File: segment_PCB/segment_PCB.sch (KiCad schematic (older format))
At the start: 36 parts, among them J2 #AVR-ISP-6, SW1 SW_Push, U4 74HC138, Y1 12MHz

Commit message: Started mock keyboard
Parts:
- removed C8, C?: 100n, Capacitor_THT:C_Disc_D3.0mm_W1.6mm_P2.50mm, symbol Device:C
- removed D4: LED, LED_THT:LED_D5.0mm, symbol Device:LED
- removed R7: R, Resistor_THT:R_Axial_DIN0204_L3.6mm_D1.6mm_P5.08mm_Horizontal, symbol Device:R
- removed SW? (x6): SW_Push, symbol Switch:SW_Push
- removed U?: 74HC138, symbol Segment_Parts:74HC138
- removed U?: 74HC365, symbol Segment_Parts:74HC365
- added C?: 100n, Capacitor_THT:C_Disc_D3.0mm_W1.6mm_P2.50mm, symbol Device:C
- added R? (x5): 10k, symbol Device:R
- added SW? (x5): SW_Push_45deg, symbol Switch:SW_Push_45deg
- added U?: 74HC365, symbol Segment_Parts:74HC365
- R6: value R -> 220R
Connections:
- net SEL4 is gone; now on net GND: U4.4 (~E1), U?.5 (~E2)
- net CBUS: now also U?.15 (~Y0), U?.15 (~E2)
- net COL1: no longer U?.6 (PD4)
- net COL2: no longer U?.11 (PD5)
- net COL3: no longer U?.12 (PD6)
- net COL4: no longer U?.13 (PD7)
- net GND: now also C?.2, U?.1 (~E1), U?.10 (A4), U?.12 (A5), U?.14 (A6), U?.2 (A1), U?.4 (A2), U?.6 (A3), U?.8 (GND)
- net LED0: now also U?.16 (PB2)
- net ROW0: now also R?.2, SW?.2
- net ROW1: now also R?.2, SW?.2
- net ROW2: now also R?.2, SW?.2
- net ROW3: now also R?.2, SW?.2
- net ROW4: now also R?.2, SW?.2
- net SEL0: now also U?.5 (PD3)
- net SEL1: now also U?.6 (PD4)
- net SEL2: now also U?.11 (PD5)
- net SEL3: now also U?.12 (PD6)
- net VCC: now also C?.1, R?.1, R?.1, R?.1, R?.1, R?.1, U?.16 (VCC)
- removed net COL0: U?.15 (~Y0), U?.5 (PD3)
- net COL14: no longer names the net of U4.9 (~Y6)
- net COL15: no longer names the net of U4.7 (~Y7)
- net ROW5: no longer names the net of U?.26 (PC3)
- new net: SW?.1, U?.11 (Y5)
- new net: SW?.1, U?.3 (Y1)
- new net: SW?.1, U?.5 (Y2)
- new net: SW?.1, U?.7 (Y3)
- new net: SW?.1, U?.9 (Y4)
- no-connect marks 2 -> 5
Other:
- moved on the sheet: C3, C4, C5, C6, C7, C?, D3, D?, F?, J2, J?, R5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

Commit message: Completed test board layout; implementing option footprints
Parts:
- U4, U?: symbol Segment_Parts:74HC138 -> Segment_Symbols:74HC138
- U?: symbol Segment_Parts:74HC365 -> Segment_Symbols:74HC365
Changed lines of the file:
@@
 	3400 2200 3400 2500
 $Comp
-L Segment_Parts:74HC138 U4
+L Segment_Symbols:74HC138 U4
 U 1 1 5FB534DC
 P 4050 2000
@@
 	13200 8600 13200 8500
 $Comp
-L Segment_Parts:74HC138 U?
+L Segment_Symbols:74HC138 U?
 U 1 1 5FBECC10
 P 1950 2000
@@
 	5400 4700 5350 4700
 $Comp
-L Segment_Parts:74HC365 U?
+L Segment_Symbols:74HC365 U?
 U 1 1 604297EC
 P 5800 5100

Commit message: Minor tweak to test board
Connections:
- net at U?.11 (Y5): now also SW?.1; no longer SW?.1
- net at U?.13 (Y6): now also SW?.1
- net at U?.3 (Y1): no longer SW?.1
- net at U?.5 (Y2): now also SW?.1; no longer SW?.1
- net at U?.7 (Y3): now also SW?.1; no longer SW?.1
- net at U?.9 (Y4): now also SW?.1; no longer SW?.1
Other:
- moved on the sheet: SW?
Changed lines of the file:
@@
 Connection ~ 13200 8300
 NoConn ~ 4450 2300
-Text GLabel 6650 5650 3    50   Input ~ 0
+Text GLabel 6600 5650 3    50   Input ~ 0
 ROW3
-Text GLabel 6850 5650 3    50   Input ~ 0
+Text GLabel 6800 5650 3    50   Input ~ 0
 ROW2
-Text GLabel 7050 5650 3    50   Input ~ 0
+Text GLabel 7000 5650 3    50   Input ~ 0
 ROW1
-Text GLabel 7250 5650 3    50   Input ~ 0
+Text GLabel 7200 5650 3    50   Input ~ 0
 ROW0
 $Comp
 L Switch:SW_Push_45deg SW?
 U 1 1 60429834
-P 7150 4800
-F 0 "SW?" V 7200 4600 50  0000 C CNN
-F 1 "SW_Push_45deg" H 7150 4990 50  0001 C CNN
-F 2 "" H 7150 4800 50  0001 C CNN
-F 3 "~" H 7150 4800 50  0001 C CNN
-	1    7150 4800
-	1    0    0    -1
-$EndComp
-Wire Wire Line
-	6650 5650 6650 5200
+P 7100 4900
+F 0 "SW?" V 7150 4700 50  0000 C CNN
+F 1 "SW_Push_45deg" H 7100 5090 50  0001 C CNN
+F 2 "" H 7100 4900 50  0001 C CNN
+F 3 "~" H 7100 4900 50  0001 C CNN
+	1    7100 4900
+	1    0    0    -1
+$EndComp
 $Comp
 L Switch:SW_Push_45deg SW?
 U 1 1 60429845
-P 6950 4900
-F 0 "SW?" V 7000 4700 50  0000 C CNN
-F 1 "SW_Push_45deg" H 6950 5090 50  0001 C CNN
-F 2 "" H 6950 4900 50  0001 C CNN
-F 3 "~" H 6950 4900 50  0001 C CNN
-	1    6950 4900
+P 6900 5000
+F 0 "SW?" V 6950 4800 50  0000 C CNN
+F 1 "SW_Push_45deg" H 6900 5190 50  0001 C CNN
+F 2 "" H 6900 5000 50  0001 C CNN
+F 3 "~" H 6900 5000 50  0001 C CNN
+	1    6900 5000
 	1    0    0    -1
 $EndComp
@@
 L Switch:SW_Push_45deg SW?
 U 1 1 6042984B
-P 6750 5000
-F 0 "SW?" V 6800 4800 50  0000 C CNN
-F 1 "SW_Push_45deg" H 6750 5190 50  0001 C CNN
-F 2 "" H 6750 5000 50  0001 C CNN
-F 3 "~" H 6750 5000 50  0001 C CNN
-	1    6750 5000
-	1    0    0    -1
-$EndComp
-Wire Wire Line
-	7250 4900 7250 5650
-Wire Wire Line
-	7050 5650 7050 5000
-Wire Wire Line
-	6850 5100 6850 5650
+P 6700 5100
+F 0 "SW?" V 6750 4900 50  0000 C CNN
+F 1 "SW_Push_45deg" H 6700 5290 50  0001 C CNN
+F 2 "" H 6700 5100 50  0001 C CNN
+F 3 "~" H 6700 5100 50  0001 C CNN
+	1    6700 5100
+	1    0    0    -1
+$EndComp
 $Comp
 L Switch:SW_Push_45deg SW?
 U 1 1 60429857
-P 6350 5200
-F 0 "SW?" V 6400 5000 50  0000 C CNN
-F 1 "SW_Push_45deg" H 6350 5390 50  0001 C CNN
-F 2 "" H 6350 5200 50  0001 C CNN
-F 3 "~" H 6350 5200 50  0001 C CNN
-	1    6350 5200
+P 6300 5300
+F 0 "SW?" V 6350 5100 50  0000 C CNN
+F 1 "SW_Push_45deg" H 6300 5490 50  0001 C CNN
+F 2 "" H 6300 5300 50  0001 C CNN
+F 3 "~" H 6300 5300 50  0001 C CNN
+	1    6300 5300
 	1    0    0    -1
 $EndComp
@@
 L Switch:SW_Push_45deg SW?
 U 1 1 60429851
-P 6550 5100
-F 0 "SW?" V 6600 4900 50  0000 C CNN
-F 1 "SW_Push_45deg" H 6550 5290 50  0001 C CNN
-F 2 "" H 6550 5100 50  0001 C CNN
-F 3 "~" H 6550 5100 50  0001 C CNN
-	1    6550 5100
-	1    0    0    -1
-$EndComp
-Wire Wire Line
-	6450 5300 6450 5650
+P 6500 5200
+F 0 "SW?" V 6550 5000 50  0000 C CNN
+F 1 "SW_Push_45deg" H 6500 5390 50  0001 C CNN
+F 2 "" H 6500 5200 50  0001 C CNN
+F 3 "~" H 6500 5200 50  0001 C CNN
+	1    6500 5200
+	1    0    0    -1
+$EndComp
 Wire Wire Line
 	5350 5400 5350 5700
@@
 Wire Wire Line
 	5350 5200 5350 5400
-Text GLabel 6450 5650 3    50   Input ~ 0
+Text GLabel 6400 5650 3    50   Input ~ 0
 ROW4
 $Comp
@@
 NoConn ~ 13100 6250
 NoConn ~ 13100 5050
-NoConn ~ 6200 5200
-Wire Wire Line
-	6200 5100 6250 5100
-Wire Wire Line
-	6200 5000 6450 5000
-Wire Wire Line
-	6200 4900 6650 4900
-Wire Wire Line
-	6200 4800 6850 4800
-Wire Wire Line
-	6200 4700 7050 4700
+NoConn ~ 6200 4700
+Wire Wire Line
+	6200 5100 6400 5100
+Wire Wire Line
+	6200 5000 6600 5000
+Wire Wire Line
+	6200 4900 6800 4900
+Wire Wire Line
+	6200 4800 7000 4800
+Wire Wire Line
+	6400 5650 6400 5400
+Wire Wire Line
+	6600 5650 6600 5300
+Wire Wire Line
+	6800 5650 6800 5200
+Wire Wire Line
+	7000 5650 7000 5100
+Wire Wire Line
+	7200 5650 7200 5000
 Wire Bus Line
 	3250 1400 3250 2200

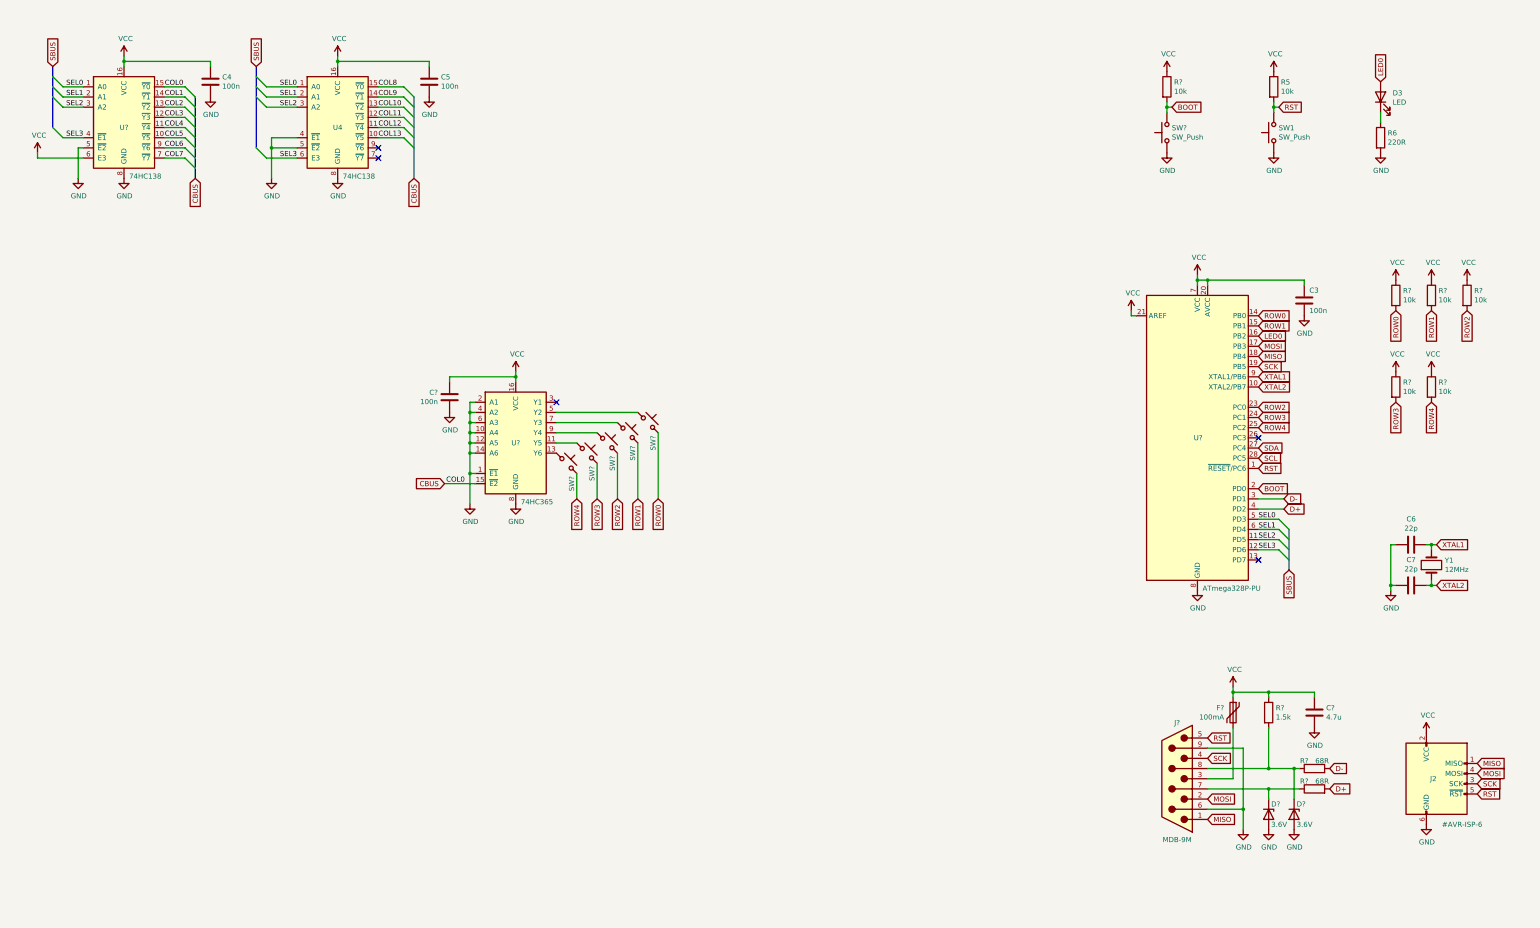
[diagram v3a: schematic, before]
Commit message: Added test board dimensions
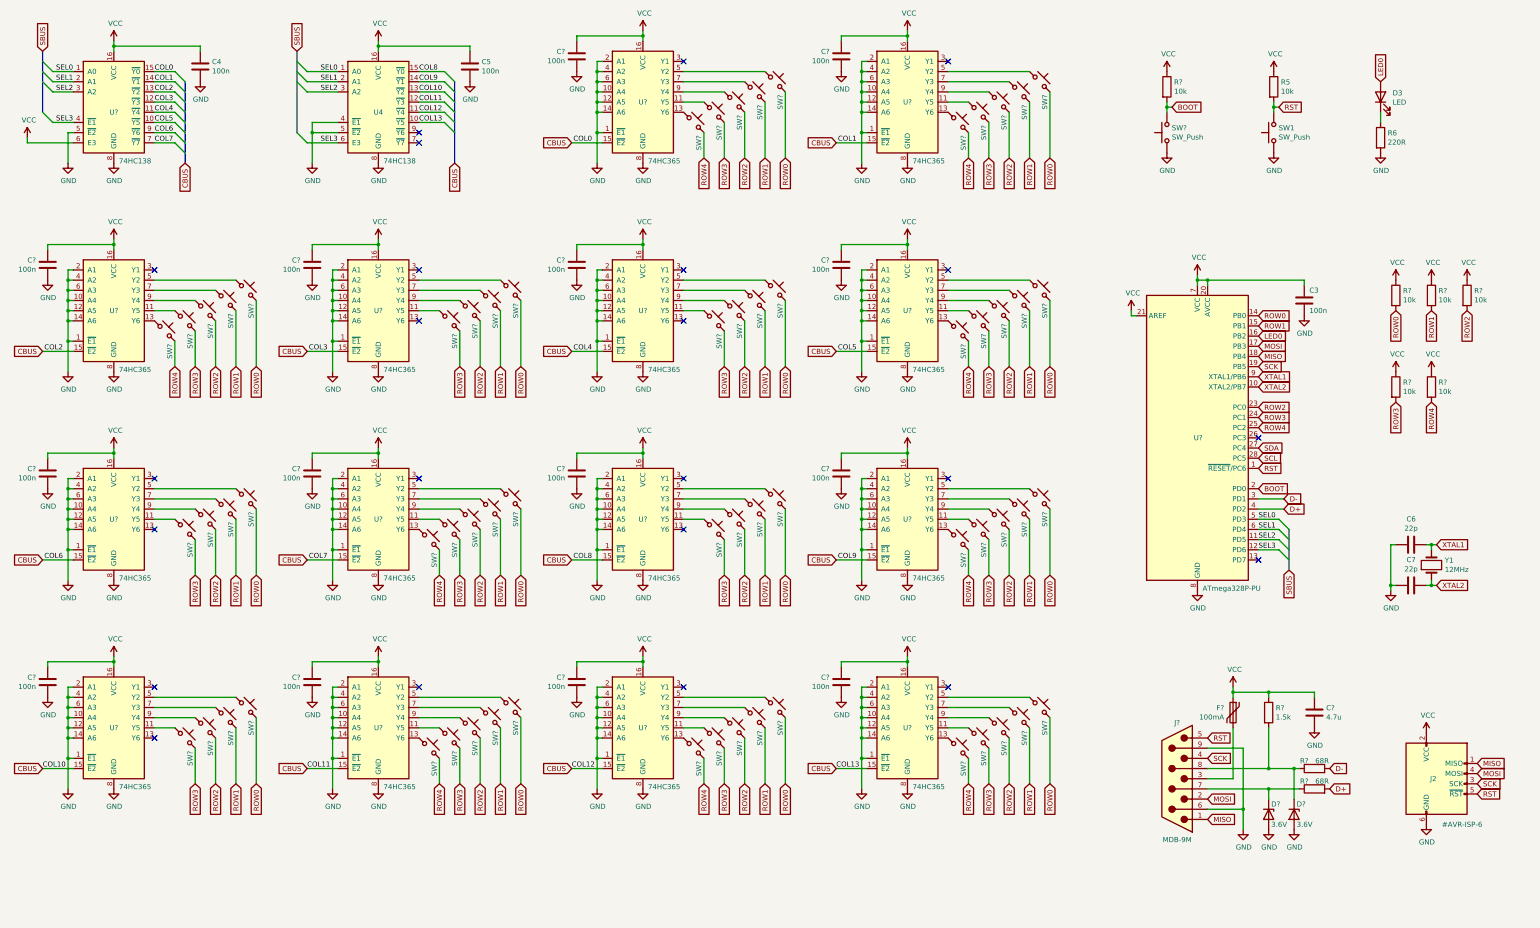
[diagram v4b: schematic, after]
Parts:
- added C? (x13): 100n, Capacitor_THT:C_Disc_D3.0mm_W1.6mm_P2.50mm, symbol Device:C
- added SW? (x60): SW_Push_45deg, symbol Switch:SW_Push_45deg
- added U? (x13): 74HC365, symbol Segment_Symbols:74HC365
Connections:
- net COL1 is gone; now on net CBUS: U?.14 (~Y1)
- net COL10 is gone; now on net CBUS: U4.13 (~Y2)
- net COL11 is gone; now on net CBUS: U4.12 (~Y3)
- net COL12 is gone; now on net CBUS: U4.11 (~Y4)
- net COL13 is gone; now on net CBUS: U4.10 (~Y5)
- net COL2 is gone; now on net CBUS: U?.13 (~Y2)
- net COL3 is gone; now on net CBUS: U?.12 (~Y3)
- net COL4 is gone; now on net CBUS: U?.11 (~Y4)
- net COL5 is gone; now on net CBUS: U?.10 (~Y5)
- net COL6 is gone; now on net CBUS: U?.9 (~Y6)
- net COL7 is gone; now on net CBUS: U?.7 (~Y7)
- net COL8 is gone; now on net CBUS: U4.15 (~Y0)
- net COL9 is gone; now on net CBUS: U4.14 (~Y1)
- net CBUS: now also U?.15 (~E2), U?.15 (~E2), U?.15 (~E2), U?.15 (~E2), U?.15 (~E2), U?.15 (~E2), U?.15 (~E2), U?.15 (~E2), U?.15 (~E2), U?.15 (~E2), U?.15 (~E2), U?.15 (~E2), U?.15 (~E2)
- net GND: now also C?.2, C?.2, C?.2, C?.2, C?.2, C?.2, C?.2, C?.2, C?.2, C?.2, C?.2, C?.2, C?.2, U?.1 (~E1), U?.1 (~E1), U?.1 (~E1), U?.1 (~E1), U?.1 (~E1), U?.1 (~E1), U?.1 (~E1), U?.1 (~E1), U?.1 (~E1), U?.1 (~E1), U?.1 (~E1), U?.1 (~E1), U?.1 (~E1), U?.10 (A4), U?.10 (A4), U?.10 (A4), U?.10 (A4), U?.10 (A4), U?.10 (A4), U?.10 (A4), U?.10 (A4), U?.10 (A4), U?.10 (A4), U?.10 (A4), U?.10 (A4), U?.10 (A4), U?.12 (A5), U?.12 (A5), U?.12 (A5), U?.12 (A5), U?.12 (A5), U?.12 (A5), U?.12 (A5), U?.12 (A5), U?.12 (A5), U?.12 (A5), U?.12 (A5), U?.12 (A5), U?.12 (A5), U?.14 (A6), U?.14 (A6), U?.14 (A6), U?.14 (A6), U?.14 (A6), U?.14 (A6), U?.14 (A6), U?.14 (A6), U?.14 (A6), U?.14 (A6), U?.14 (A6), U?.14 (A6), U?.14 (A6), U?.2 (A1), U?.2 (A1), U?.2 (A1), U?.2 (A1), U?.2 (A1), U?.2 (A1), U?.2 (A1), U?.2 (A1), U?.2 (A1), U?.2 (A1), U?.2 (A1), U?.2 (A1), U?.2 (A1), U?.4 (A2), U?.4 (A2), U?.4 (A2), U?.4 (A2), U?.4 (A2), U?.4 (A2), U?.4 (A2), U?.4 (A2), U?.4 (A2), U?.4 (A2), U?.4 (A2), U?.4 (A2), U?.4 (A2), U?.6 (A3), U?.6 (A3), U?.6 (A3), U?.6 (A3), U?.6 (A3), U?.6 (A3), U?.6 (A3), U?.6 (A3), U?.6 (A3), U?.6 (A3), U?.6 (A3), U?.6 (A3), U?.6 (A3), U?.8 (GND), U?.8 (GND), U?.8 (GND), U?.8 (GND), U?.8 (GND), U?.8 (GND), U?.8 (GND), U?.8 (GND), U?.8 (GND), U?.8 (GND), U?.8 (GND), U?.8 (GND), U?.8 (GND)
- net ROW0: now also SW?.2, SW?.2, SW?.2, SW?.2, SW?.2, SW?.2, SW?.2, SW?.2, SW?.2, SW?.2, SW?.2, SW?.2, SW?.2
- net ROW1: now also SW?.2, SW?.2, SW?.2, SW?.2, SW?.2, SW?.2, SW?.2, SW?.2, SW?.2, SW?.2, SW?.2, SW?.2, SW?.2
- net ROW2: now also SW?.2, SW?.2, SW?.2, SW?.2, SW?.2, SW?.2, SW?.2, SW?.2, SW?.2, SW?.2, SW?.2, SW?.2, SW?.2
- net ROW3: now also SW?.2, SW?.2, SW?.2, SW?.2, SW?.2, SW?.2, SW?.2, SW?.2, SW?.2, SW?.2, SW?.2, SW?.2, SW?.2
- net ROW4: now also SW?.2, SW?.2, SW?.2, SW?.2, SW?.2, SW?.2, SW?.2, SW?.2
- net VCC: now also C?.1, C?.1, C?.1, C?.1, C?.1, C?.1, C?.1, C?.1, C?.1, C?.1, C?.1, C?.1, C?.1, U?.16 (VCC), U?.16 (VCC), U?.16 (VCC), U?.16 (VCC), U?.16 (VCC), U?.16 (VCC), U?.16 (VCC), U?.16 (VCC), U?.16 (VCC), U?.16 (VCC), U?.16 (VCC), U?.16 (VCC), U?.16 (VCC)
- new net: SW?.1, U?.11 (Y5) (x13)
- new net: SW?.1, U?.13 (Y6) (x8)
- new net: SW?.1, U?.5 (Y2) (x13)
- new net: SW?.1, U?.7 (Y3) (x13)
- new net: SW?.1, U?.9 (Y4) (x13)
- no-connect marks 5 -> 23
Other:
- moved on the sheet: C4, C5, C?, SW?, U4, U?
